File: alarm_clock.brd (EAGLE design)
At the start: 100 x 80 mm, 32 parts, among them IC1 ATMEGA328P-PU, IC2 MC14489BPE, IC3 DS3231, Q1 16MHz

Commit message: Replaced toggle switch & green led with connectors:
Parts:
- removed ALARM: S1, switch:320-916
- removed LED3: Green, led:LED3MM
- added ALARM_TOGGLE: (no value), pinhead:1X03/90
- SNOOZE: device pinhead:1X03/90 -> pinhead:1X05/90
- moved SNOOZE 3.82 mm to (31.8, 68.6), flipped to the top
- moved BATT 2.54 mm to (52.1, 69.5)
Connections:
- removed net B: D1.6, D2.6, D3.6, D4.6, IC2.6, LED3.A
- new net GREEN_LED: D1.6, D2.6, D3.6, D4.6, IC2.6, SNOOZE.4
- new net LED: SNOOZE.5
- net GND: now also ALARM_TOGGLE.2, SNOOZE.3; no longer ALARM.2, SNOOZE.2
- net LEDS: no longer LED3.K
- net N$2: now also SNOOZE.1; no longer SNOOZE.3
- net N$5: now also ALARM_TOGGLE.3; no longer ALARM.1
- net N$6: now also ALARM_TOGGLE.1; no longer ALARM.3
- net N$9: now also SNOOZE.2; no longer SNOOZE.1
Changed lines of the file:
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@@
 </autorouter>
 <elements>
-<element name="ALARM" library="switch" package="320-916" value="S1" x="93.98" y="12.7" rot="R180"/>
-<element name="BATT" library="adafruit" package="CR2032-THRU" value="CR2032" x="49.53" y="69.5325" rot="MR0">
-<attribute name="MPN" value="1066.." x="49.53" y="69.5325" size="1.778" layer="28" rot="MR0" display="off"/>
-<attribute name="MF" value="KEYSTONE" x="49.53" y="69.5325" size="1.778" layer="28" rot="MR0" display="off"/>
-<attribute name="OC_FARNELL" value="2293258" x="49.53" y="69.5325" size="1.778" layer="28" rot="MR0" display="off"/>
+<element name="BATT" library="adafruit" package="CR2032-THRU" value="CR2032" x="52.07" y="69.5325" rot="MR0">
+<attribute name="MPN" value="1066.." x="52.07" y="69.5325" size="1.778" layer="28" rot="MR0" display="off"/>
+<attribute name="MF" value="KEYSTONE" x="52.07" y="69.5325" size="1.778" layer="28" rot="MR0" display="off"/>
+<attribute name="OC_FARNELL" value="2293258" x="52.07" y="69.5325" size="1.778" layer="28" rot="MR0" display="off"/>
 </element>
 <element name="C1" library="rcl" package="C025-024X044" value="22pF" x="73.9775" y="44.7675" smashed="yes">
@@
 <attribute name="MF" value="MULTICOMP" x="48.895" y="14.605" size="1.778" layer="27" display="off"/>
 <attribute name="OC_FARNELL" value="1581228" x="48.895" y="14.605" size="1.778" layer="27" display="off"/>
-</element>
-<element name="LED3" library="led" package="LED3MM" value="Green" x="83.82" y="12.7">
-<attribute name="MPN" value="L-1503GC" x="83.82" y="12.7" size="1.778" layer="27" display="off"/>
-<attribute name="MF" value="KINGBRIGHT" x="83.82" y="12.7" size="1.778" layer="27" display="off"/>
-<attribute name="OC_FARNELL" value="2335730" x="83.82" y="12.7" size="1.778" layer="27" display="off"/>
 </element>
 <element name="PH2" library="photo-elements" package="T0-46-A10XX" value="" x="12.7" y="73.66" rot="R180">
@@
 <attribute name="VALUE" x="13.6906" y="29.5275" size="2.0828" layer="27" ratio="10" rot="SR0"/>
 </element>
-<element name="SNOOZE" library="pinhead" package="1X03/90" value="" x="28.8925" y="66.04" rot="MR0"/>
 <element name="IC3" library="ds3231" package="DS3231-8_SO" value="DS3231" x="49.53" y="46.99" rot="R90"/>
+<element name="ALARM_TOGGLE" library="pinhead" package="1X03/90" value="" x="93.0275" y="11.43"/>
+<element name="SNOOZE" library="pinhead" package="1X05/90" value="" x="31.75" y="68.58"/>
 </elements>
 <signals>
@@
 <contactref element="BATT" pad="-"/>
 <contactref element="C3" pad="2"/>
-<contactref element="ALARM" pad="2"/>
 <contactref element="S2" pad="1"/>
 <contactref element="S2" pad="2"/>
 <contactref element="J2" pad="5"/>
 <contactref element="J2" pad="P$1"/>
-<contactref element="SNOOZE" pad="2"/>
 <contactref element="IC3" pad="5"/>
 <polygon width="0.4064" layer="16">
@@
 <vertex x="100.33" y="80.01"/>
 </polygon>
-<wire x1="50.8" y1="57.15" x2="50.48" y2="49.4425" width="0" layer="19" extent="1-1"/>
+<contactref element="ALARM_TOGGLE" pad="2"/>
+<contactref element="SNOOZE" pad="3"/>
+<wire x1="96.38" y1="50.135" x2="97.155" y2="55.535" width="0" layer="19" extent="1-1"/>
+<wire x1="97.5487" y1="41.9481" x2="96.38" y2="50.135" width="0" layer="19" extent="1-1"/>
+<wire x1="91.0463" y1="41.9481" x2="97.5487" y2="41.9481" width="0" layer="19" extent="1-1"/>
+<wire x1="74.93" y1="34.29" x2="91.0463" y2="41.9481" width="0" layer="19" extent="1-1"/>
+<wire x1="77.47" y1="26.67" x2="74.93" y2="34.29" width="0" layer="19" extent="1-1"/>
+<wire x1="72.7075" y1="44.7675" x2="74.93" y2="34.29" width="0" layer="19" extent="1-1"/>
+<wire x1="68.8975" y1="44.7675" x2="72.7075" y2="44.7675" width="0" layer="19" extent="1-1"/>
+<wire x1="67.6275" y1="62.23" x2="68.8975" y2="44.7675" width="0" layer="19" extent="1-1"/>
+<wire x1="80.3275" y1="62.23" x2="67.6275" y2="62.23" width="0" layer="19" extent="1-1"/>
+<wire x1="50.8" y1="57.15" x2="67.6275" y2="62.23" width="0" layer="19" extent="1-1"/>
+<wire x1="50.48" y1="49.4425" x2="50.8" y2="57.15" width="0" layer="19" extent="1-1"/>
+<wire x1="50.8" y1="40.64" x2="50.48" y2="49.4425" width="0" layer="19" extent="1-1"/>
+<wire x1="52.07" y1="69.5325" x2="50.8" y2="57.15" width="0" layer="19" extent="16-16"/>
+<wire x1="93.0275" y1="7.62" x2="77.47" y2="26.67" width="0" layer="19" extent="1-1"/>
+<wire x1="19.05" y1="26.67" x2="50.8" y2="40.64" width="0" layer="19" extent="1-1"/>
+<wire x1="31.75" y1="64.77" x2="19.05" y2="26.67" width="0" layer="19" extent="1-1"/>
+<wire x1="11.43" y1="54.61" x2="19.05" y2="26.67" width="0" layer="19" extent="1-1"/>
+<wire x1="5.3975" y1="67.31" x2="11.43" y2="54.61" width="0" layer="19" extent="1-1"/>
+<wire x1="11" y1="73.66" x2="5.3975" y2="67.31" width="0" layer="19" extent="1-1"/>
 </signal>
 <signal name="N$14">
@@
 <wire x1="19.05" y1="34.29" x2="28.8925" y2="20.32" width="0" layer="19" extent="1-1"/>
 </signal>
-<signal name="B">
+<signal name="GREEN_LED">
 <contactref element="IC2" pad="6"/>
 <contactref element="D1" pad="6"/>
@@
 <contactref element="D3" pad="6"/>
 <contactref element="D4" pad="6"/>
-<contactref element="LED3" pad="A"/>
-<wire x1="82.55" y1="12.7" x2="76.2" y2="20.32" width="0" layer="19" extent="1-1"/>
+<contactref element="SNOOZE" pad="4"/>
 <wire x1="63.8175" y1="20.32" x2="76.2" y2="20.32" width="0" layer="19" extent="1-1"/>
 <wire x1="43.815" y1="20.32" x2="63.8175" y2="20.32" width="0" layer="19" extent="1-1"/>
 <wire x1="31.4325" y1="20.32" x2="43.815" y2="20.32" width="0" layer="19" extent="1-1"/>
 <wire x1="21.59" y1="34.29" x2="31.4325" y2="20.32" width="0" layer="19" extent="1-1"/>
+<wire x1="34.29" y1="64.77" x2="31.4325" y2="20.32" width="0" layer="19" extent="1-1"/>
 </signal>
 <signal name="C">
@@
 <contactref element="IC2" pad="17"/>
 <contactref element="LED2" pad="K"/>
-<contactref element="LED3" pad="K"/>
 <contactref element="LED1" pad="K"/>
-<wire x1="50.165" y1="14.605" x2="85.09" y2="12.7" width="0" layer="19" extent="1-1"/>
 <wire x1="50.165" y1="10.16" x2="50.165" y2="14.605" width="0" layer="19" extent="1-1"/>
 <wire x1="26.67" y1="26.67" x2="50.165" y2="14.605" width="0" layer="19" extent="1-1"/>
@@
 <contactref element="C5" pad="1"/>
 <contactref element="IC3" pad="6"/>
-<wire x1="48.26" y1="57.15" x2="60.198" y2="69.5325" width="0" layer="19" extent="1-1"/>
+<wire x1="48.26" y1="57.15" x2="62.738" y2="69.5325" width="0" layer="19" extent="1-1"/>
 <wire x1="49.83" y1="49.4425" x2="48.26" y2="57.15" width="0" layer="19" extent="1-1"/>
-<wire x1="38.862" y1="69.5325" x2="48.26" y2="57.15" width="0" layer="19" extent="1-1"/>
+<wire x1="41.402" y1="69.5325" x2="48.26" y2="57.15" width="0" layer="19" extent="1-1"/>
 </signal>
 <signal name="N$1">
@@
 <signal name="N$5">
 <contactref element="IC1" pad="23"/>
-<contactref element="ALARM" pad="1"/>
-<wire x1="93.98" y1="8.6868" x2="80.01" y2="26.67" width="0" layer="19" extent="1-1"/>
+<contactref element="ALARM_TOGGLE" pad="3"/>
+<wire x1="95.5675" y1="7.62" x2="80.01" y2="26.67" width="0" layer="19" extent="1-1"/>
 </signal>
 <signal name="N$6">
-<contactref element="ALARM" pad="3"/>
 <contactref element="IC1" pad="24"/>
-<wire x1="82.55" y1="26.67" x2="93.98" y2="16.7132" width="0" layer="19" extent="1-1"/>
+<contactref element="ALARM_TOGGLE" pad="1"/>
+<wire x1="90.4875" y1="7.62" x2="82.55" y2="26.67" width="0" layer="19" extent="1-1"/>
 </signal>
 <signal name="N$9">
 <contactref element="IC1" pad="25"/>
-<contactref element="SNOOZE" pad="1"/>
-<wire x1="31.4325" y1="62.23" x2="85.09" y2="26.67" width="0" layer="19" extent="1-1"/>
+<contactref element="SNOOZE" pad="2"/>
+<wire x1="29.21" y1="64.77" x2="85.09" y2="26.67" width="0" layer="19" extent="1-1"/>
 </signal>
 <signal name="RESET">
@@
 </signal>
 <signal name="N$2">
-<contactref element="SNOOZE" pad="3"/>
 <contactref element="R4" pad="2"/>
-<wire x1="25.0825" y1="57.785" x2="26.3525" y2="62.23" width="0" layer="19" extent="1-1"/>
+<contactref element="SNOOZE" pad="1"/>
+<wire x1="26.67" y1="64.77" x2="25.0825" y2="57.785" width="0" layer="19" extent="1-1"/>
+</signal>
+<signal name="LED">
+<contactref element="SNOOZE" pad="5"/>
 </signal>
 </signals>

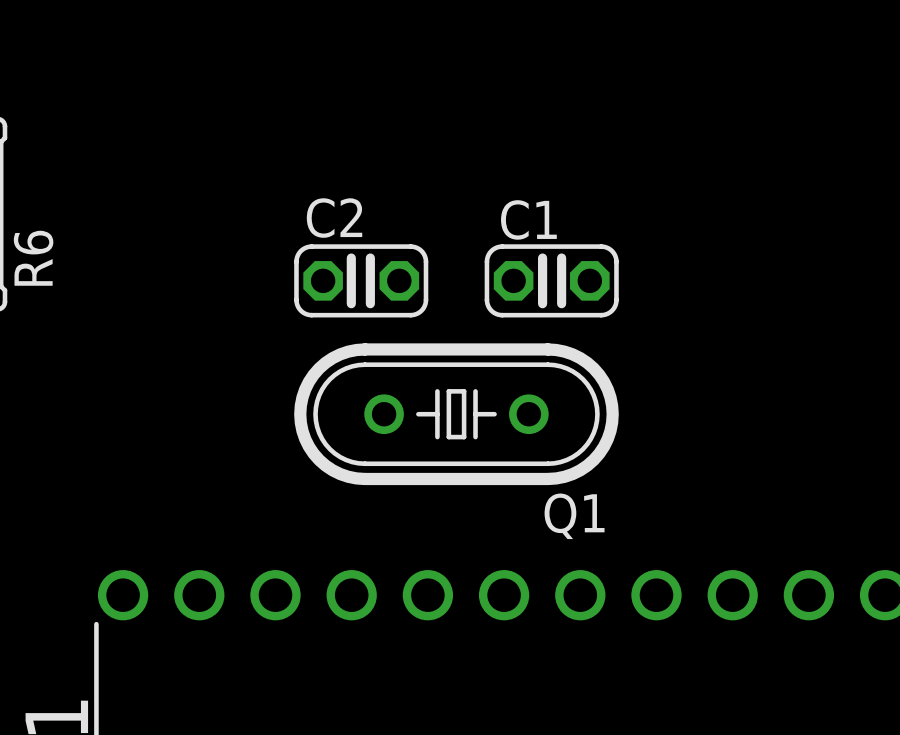
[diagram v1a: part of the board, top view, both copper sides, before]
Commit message: crystal oscilator omitted form schematic/board:
internal oscilator of atmega328p to be used ths reducing parts count:
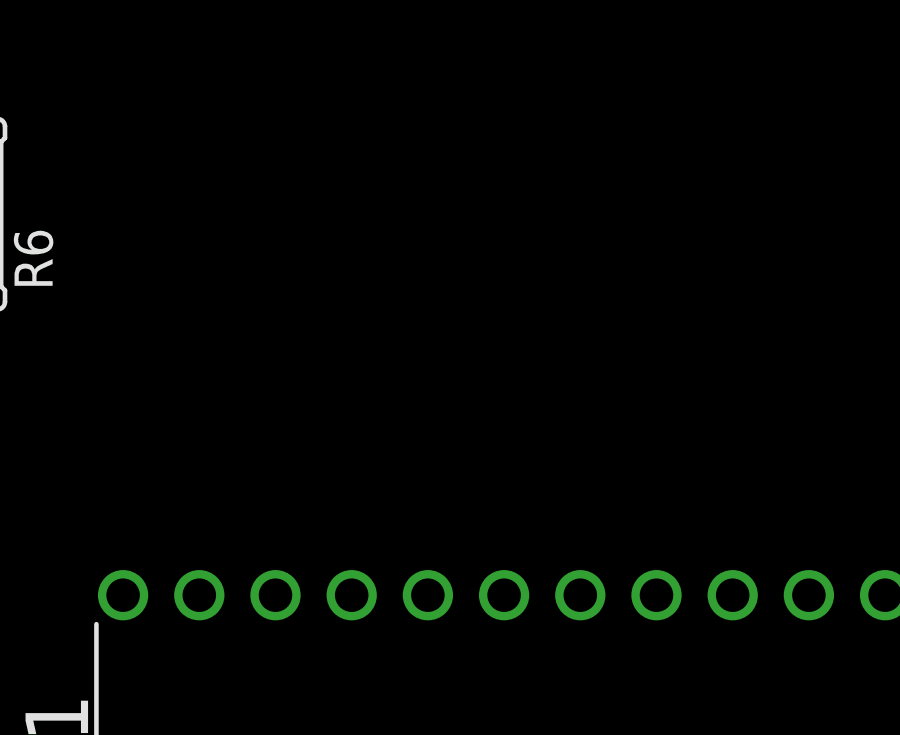
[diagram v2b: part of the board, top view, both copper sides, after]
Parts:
- removed C1, C2: 22pF, rcl:C025-024X044
- removed Q1: 16MHz, crystal:HC49/S
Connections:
- removed net N$18: C2.2, IC1.10, Q1.2
- removed net N$19: C1.2, IC1.9, Q1.1
- net DATA: no longer IC1.14
- net GND: no longer C1.1, C2.1
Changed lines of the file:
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@@
 <?xml version="1.0" encoding="utf-8"?>
 <!DOCTYPE eagle SYSTEM "eagle.dtd">
-<eagle version="7.6.0">
+<eagle version="7.7.0">
 <drawing>
 <settings>
@@
 <attribute name="OC_FARNELL" value="2293258" x="52.07" y="69.5325" size="1.778" layer="28" rot="MR0" display="off"/>
 </element>
-<element name="C1" library="rcl" package="C025-024X044" value="22pF" x="73.9775" y="44.7675" smashed="yes">
-<attribute name="MPN" value="" x="73.9775" y="44.7675" size="1.778" layer="27" display="off"/>
-<attribute name="MF" value="" x="73.9775" y="44.7675" size="1.778" layer="27" display="off"/>
-<attribute name="OC_FARNELL" value="unknown" x="73.9775" y="44.7675" size="1.778" layer="27" display="off"/>
-<attribute name="NAME" x="72.1995" y="46.1645" size="1.27" layer="25" ratio="10"/>
-</element>
-<element name="C2" library="rcl" package="C025-024X044" value="22pF" x="67.6275" y="44.7675" smashed="yes" rot="R180">
-<attribute name="MPN" value="" x="67.6275" y="44.7675" size="1.778" layer="27" rot="R180" display="off"/>
-<attribute name="MF" value="" x="67.6275" y="44.7675" size="1.778" layer="27" rot="R180" display="off"/>
-<attribute name="OC_FARNELL" value="unknown" x="67.6275" y="44.7675" size="1.778" layer="27" rot="R180" display="off"/>
-<attribute name="NAME" x="67.818" y="47.498" size="1.27" layer="25" ratio="10" rot="R180"/>
-</element>
 <element name="C3" library="rcl" package="C025-024X044" value="1uF" x="49.53" y="40.64" smashed="yes">
 <attribute name="MPN" value="" x="49.53" y="40.64" size="1.778" layer="27" display="off"/>
@@
 <attribute name="MF" value="" x="81.5975" y="66.04" size="1.778" layer="28" rot="MR0" display="off"/>
 <attribute name="OC_FARNELL" value="unknown" x="81.5975" y="66.04" size="1.778" layer="28" rot="MR0" display="off"/>
-</element>
-<element name="Q1" library="crystal" package="HC49/S" value="16MHz" x="70.8025" y="40.3225" smashed="yes" rot="R180">
-<attribute name="MPN" value="HC49SM-3.6864-30-50-60-16-ATF" x="70.8025" y="40.3225" size="1.778" layer="27" rot="R180" display="off"/>
-<attribute name="MF" value="MULTICOMP" x="70.8025" y="40.3225" size="1.778" layer="27" rot="R180" display="off"/>
-<attribute name="OC_FARNELL" value="1667008" x="70.8025" y="40.3225" size="1.778" layer="27" rot="R180" display="off"/>
-<attribute name="OC_NEWARK" value="unknown" x="70.8025" y="40.3225" size="1.778" layer="27" rot="R180" display="off"/>
-<attribute name="NAME" x="75.8825" y="37.6555" size="1.27" layer="25" ratio="10" rot="R180"/>
 </element>
 <element name="R1" library="pot" package="CA6V" value="10kΩ" x="12.7" y="63.5" smashed="yes">
@@
 <contactref element="PIEZO" pad="2"/>
 <contactref element="D5" pad="A"/>
-<contactref element="C2" pad="1"/>
-<contactref element="C1" pad="1"/>
 <contactref element="C5" pad="2"/>
 <contactref element="BATT" pad="-"/>
@@
 <wire x1="74.93" y1="34.29" x2="91.0463" y2="41.9481" width="0" layer="19" extent="1-1"/>
 <wire x1="77.47" y1="26.67" x2="74.93" y2="34.29" width="0" layer="19" extent="1-1"/>
-<wire x1="72.7075" y1="44.7675" x2="74.93" y2="34.29" width="0" layer="19" extent="1-1"/>
-<wire x1="68.8975" y1="44.7675" x2="72.7075" y2="44.7675" width="0" layer="19" extent="1-1"/>
-<wire x1="67.6275" y1="62.23" x2="68.8975" y2="44.7675" width="0" layer="19" extent="1-1"/>
-<wire x1="80.3275" y1="62.23" x2="67.6275" y2="62.23" width="0" layer="19" extent="1-1"/>
-<wire x1="50.8" y1="57.15" x2="67.6275" y2="62.23" width="0" layer="19" extent="1-1"/>
+<wire x1="80.3275" y1="62.23" x2="97.155" y2="55.535" width="0" layer="19" extent="1-1"/>
+<wire x1="67.6275" y1="62.23" x2="80.3275" y2="62.23" width="0" layer="19" extent="1-1"/>
+<wire x1="52.07" y1="69.5325" x2="67.6275" y2="62.23" width="0" layer="19" extent="16-16"/>
+<wire x1="50.8" y1="57.15" x2="52.07" y2="69.5325" width="0" layer="19" extent="16-16"/>
 <wire x1="50.48" y1="49.4425" x2="50.8" y2="57.15" width="0" layer="19" extent="1-1"/>
 <wire x1="50.8" y1="40.64" x2="50.48" y2="49.4425" width="0" layer="19" extent="1-1"/>
-<wire x1="52.07" y1="69.5325" x2="50.8" y2="57.15" width="0" layer="19" extent="16-16"/>
+<wire x1="31.75" y1="64.77" x2="50.8" y2="57.15" width="0" layer="19" extent="1-1"/>
+<wire x1="11" y1="73.66" x2="31.75" y2="64.77" width="0" layer="19" extent="1-1"/>
+<wire x1="5.3975" y1="67.31" x2="11" y2="73.66" width="0" layer="19" extent="1-1"/>
+<wire x1="11.43" y1="54.61" x2="5.3975" y2="67.31" width="0" layer="19" extent="1-1"/>
 <wire x1="93.0275" y1="7.62" x2="77.47" y2="26.67" width="0" layer="19" extent="1-1"/>
-<wire x1="19.05" y1="26.67" x2="50.8" y2="40.64" width="0" layer="19" extent="1-1"/>
-<wire x1="31.75" y1="64.77" x2="19.05" y2="26.67" width="0" layer="19" extent="1-1"/>
-<wire x1="11.43" y1="54.61" x2="19.05" y2="26.67" width="0" layer="19" extent="1-1"/>
-<wire x1="5.3975" y1="67.31" x2="11.43" y2="54.61" width="0" layer="19" extent="1-1"/>
-<wire x1="11" y1="73.66" x2="5.3975" y2="67.31" width="0" layer="19" extent="1-1"/>
+<wire x1="19.05" y1="26.67" x2="11.43" y2="54.61" width="0" layer="19" extent="1-1"/>
 </signal>
 <signal name="N$14">
@@
 <wire x1="75.2475" y1="62.23" x2="82.8675" y2="62.23" width="0" layer="19" extent="1-1"/>
 <wire x1="73.66" y1="67.31" x2="75.2475" y2="62.23" width="0" layer="19" extent="1-1"/>
-</signal>
-<signal name="N$18">
-<contactref element="C2" pad="2"/>
-<contactref element="Q1" pad="2"/>
-<contactref element="IC1" pad="10"/>
-<wire x1="68.3895" y1="40.3225" x2="66.3575" y2="44.7675" width="0" layer="19" extent="1-1"/>
-<wire x1="69.85" y1="34.29" x2="68.3895" y2="40.3225" width="0" layer="19" extent="1-1"/>
-</signal>
-<signal name="N$19">
-<contactref element="C1" pad="2"/>
-<contactref element="Q1" pad="1"/>
-<contactref element="IC1" pad="9"/>
-<wire x1="73.2155" y1="40.3225" x2="75.2475" y2="44.7675" width="0" layer="19" extent="1-1"/>
-<wire x1="72.39" y1="34.29" x2="73.2155" y2="40.3225" width="0" layer="19" extent="1-1"/>
 </signal>
 <signal name="N$21">
@@
 </signal>
 <signal name="DATA">
-<contactref element="IC1" pad="14"/>
 <contactref element="IC2" pad="12"/>
-<wire x1="13.97" y1="26.67" x2="59.69" y2="34.29" width="0" layer="19" extent="1-1"/>
 </signal>
 <signal name="CLK">
